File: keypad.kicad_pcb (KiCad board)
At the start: 2 copper layers, 76.3 x 115.3 mm, 104 parts, among them IC1 IS31FL3733-TQLS4, J1 Conn_01x04_Female, J3 B3FS-1002P, J4 USB_C_Receptacle_USB2.0, K1_1 KEYSW, K1_2 KEYSW, K1_3 KEYSW, K1_4 KEYSW, K2_1 KEYSW, K2_2 KEYSW, K2_3 KEYSW, K2_4 KEYSW, K3_1 KEYSW, K3_2 KEYSW, K3_3 KEYSW, K3_4 KEYSW, K4_1 KEYSW, K4_2 KEYSW, K4_3 KEYSW, K4_4 KEYSW, K5_1 KEYSW, K5_2 KEYSW, K5_3 KEYSW, U1 ATMEGA32U4, Y1 Crystal_GND24

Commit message: first manufactured version, testing needed
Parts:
- removed D12, D15, D17, D19, D20, D22: SK6805, LED_SMD:LED_SK6812MINI_PLCC4_3.5x3.5mm_P1.75mm
- added G***: LOGO, decals:science_badge, B.Cu at (173.5, 144.9)
- added G***: LOGO, decals:nostromo, B.Cu at (145.9, 99.8)
- J4: footprint Connector_USB:USB_C_Receptacle_Amphenol_12401548E4-2A_CircularHoles -> USB_C:Wuerth USB3.1 Type C Receptacle - Horizontal
- moved D16 14.5 mm to (111.7, 94.1)
- moved D13 14.3 mm to (179.5, 40.3)
- moved D14 13.6 mm to (114.6, 40.1)
- moved D23 12.6 mm to (181.2, 92.5)
- moved D18 11.5 mm to (111.5, 143.0)
- moved D21 9.45 mm to (179.6, 139.0)
- moved J4 5.07 mm to (142.7, 35.2)
- moved G*** 3.89 mm to (131.9, 55.8)
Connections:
- D13 pad 3: Net-(D12-Pad1) -> /led/UGLOW_LED
- D16 pad 3: Net-(D15-Pad1) -> Net-(D14-Pad1)
- D18 pad 3: Net-(D17-Pad1) -> Net-(D16-Pad1)
- D21 pad 3: Net-(D20-Pad1) -> Net-(D18-Pad1)
- D23 pad 3: Net-(D22-Pad1) -> Net-(D21-Pad1)
- J4 pad S1: GND -> (no net)
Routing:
- net Net-(D18-Pad1): track 30.5 -> 82.7 mm
- net Net-(D19-Pad1): track 34.5 -> 0.00 mm
- net Net-(D12-Pad1): track 30.1 -> 0.00 mm
- net Net-(D13-Pad1): track 35.2 -> 62.8 mm
- net +5V: track 477.7 -> 452.7 mm, vias 11 -> 10
- net Net-(D20-Pad1): track 24.1 -> 0.00 mm
- net Net-(D22-Pad1): track 24.0 -> 0.00 mm
- net GND: track 114.0 -> 90.3 mm, vias 44 -> 32
- net Net-(D21-Pad1): track 21.2 -> 44.5 mm
- net Net-(D14-Pad1): track 30.8 -> 52.9 mm
- net Net-(D15-Pad1): track 21.6 -> 0.00 mm
- net Net-(D17-Pad1): track 21.4 -> 0.00 mm
- net Net-(D16-Pad1): track 25.0 -> 46.2 mm
- net /led/UGLOW_LED: track 21.3 -> 7.16 mm
- net /CC1: track 13.8 -> 11.9 mm
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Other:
- board text added: "©FM 2019"

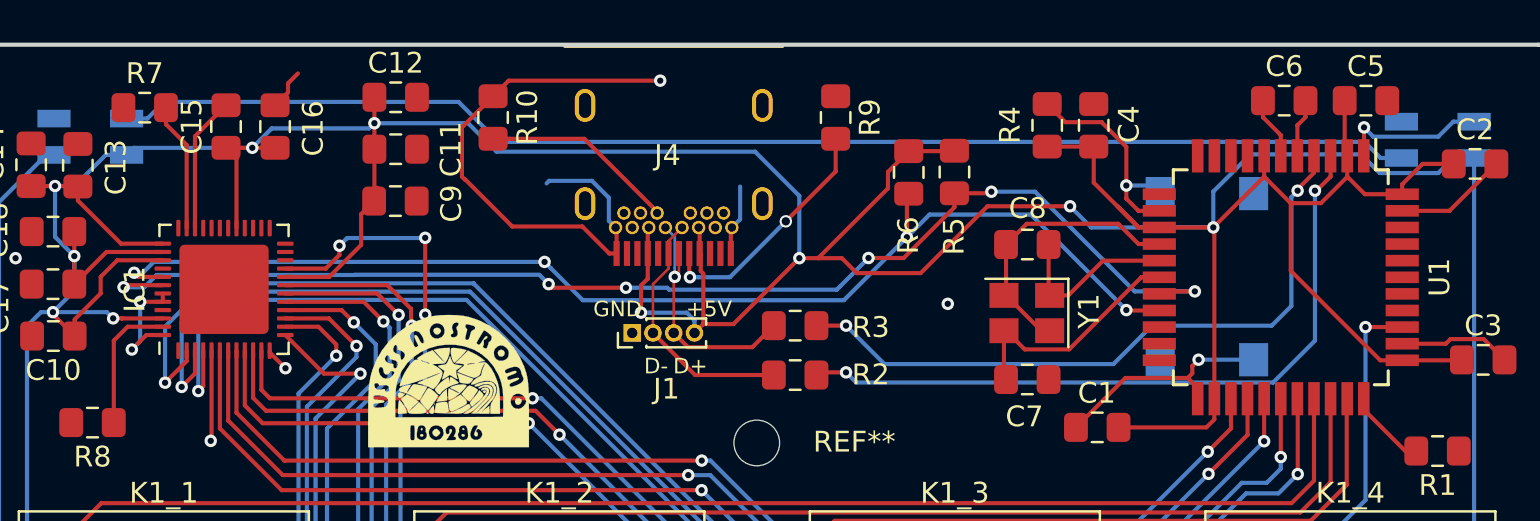
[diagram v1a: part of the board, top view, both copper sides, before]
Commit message: rerouted D+ and D- lines
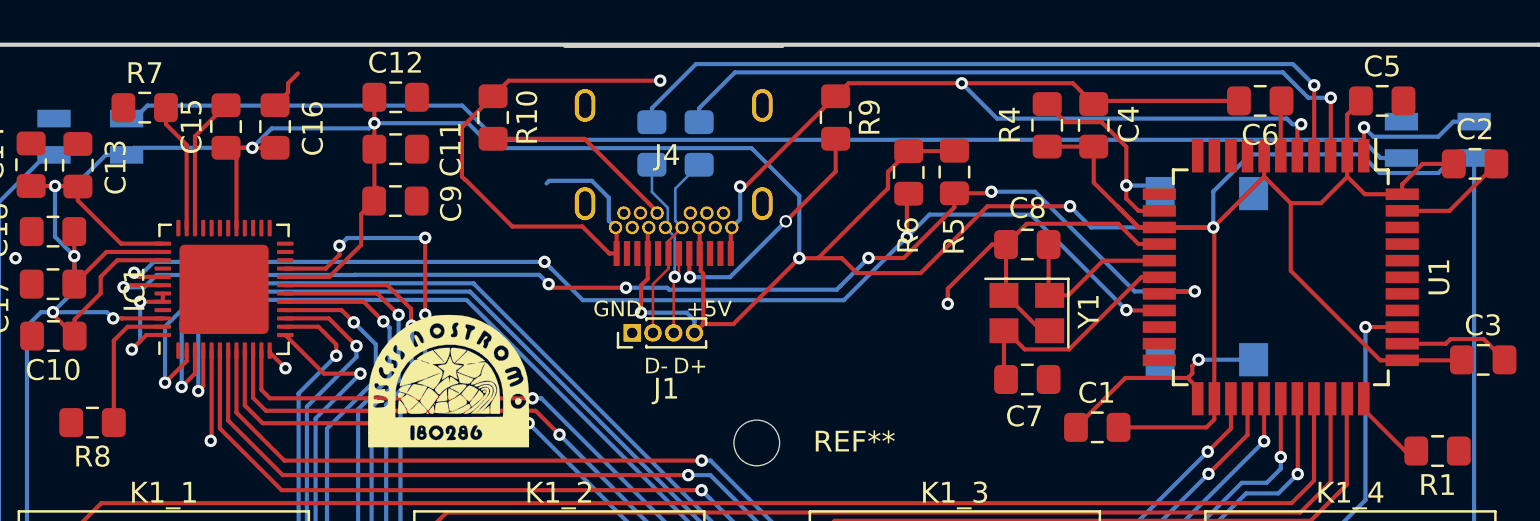
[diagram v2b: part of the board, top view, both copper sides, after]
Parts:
- R2, R3: moved to B.Cu
- moved R2 12.1 mm to (143.9, 40.5), turned to 270 degrees
- moved R3 11.2 mm to (141.7, 40.5), turned to 270 degrees
- moved C6 1.16 mm to (170.9, 38.4), turned to 180 degrees
- moved C5 0.78 mm to (176.8, 38.4)
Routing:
- net GND: track 90.3 -> 137.2 mm, vias 32 -> 35
- net Net-(R3-Pad1): track 32.5 -> 37.3 mm, vias 2 -> 1
- net /USB_D-: track 12.3 -> 9.29 mm
- net /USB_D+: track 12.0 -> 9.88 mm
- net Net-(R2-Pad1): track 34.4 -> 35.1 mm, vias 2 -> 1

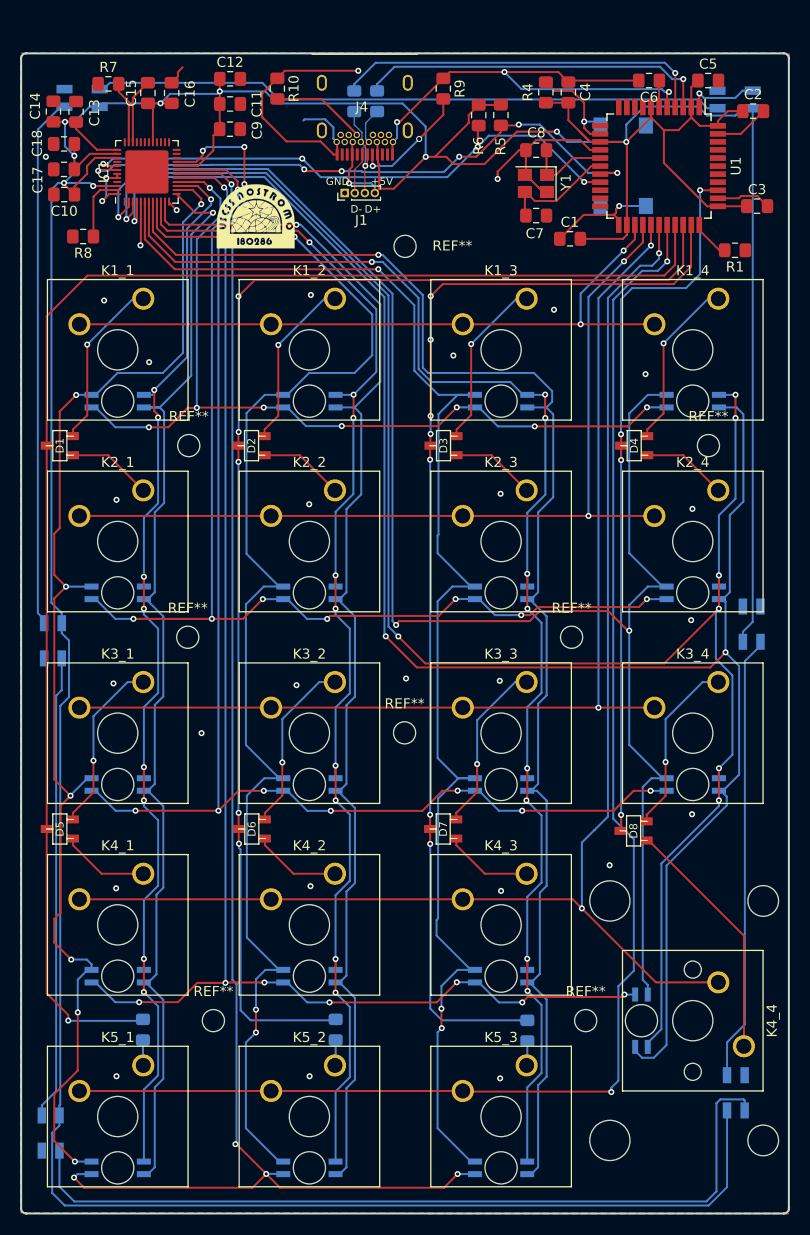
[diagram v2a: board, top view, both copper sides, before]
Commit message: Auf STM32F303 Controller umgestiegen. RGB per Switch rausgeflogen.
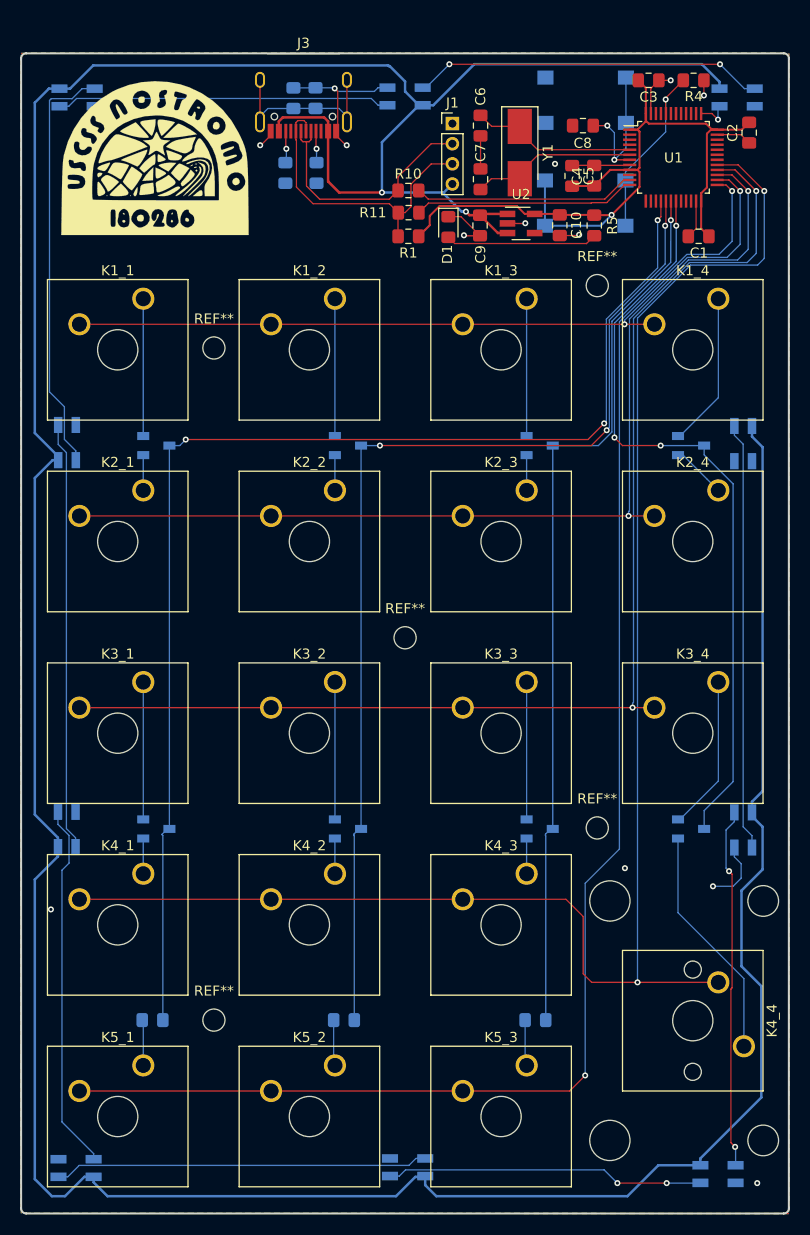
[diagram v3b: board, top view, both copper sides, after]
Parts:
- removed C12: 22uF, Capacitor_SMD:C_0805_2012Metric_Pad1.15x1.40mm_HandSolder
- removed C13, C15, C17: 0.1uF, Capacitor_SMD:C_0805_2012Metric_Pad1.15x1.40mm_HandSolder
- removed C14, C16, C18: 0.47uF, Capacitor_SMD:C_0805_2012Metric_Pad1.15x1.40mm_HandSolder
- removed D23: SK6805, LED_SMD:LED_SK6812MINI_PLCC4_3.5x3.5mm_P1.75mm
- removed D_LED_1, D_LED_10, D_LED_11, D_LED_12, D_LED_13, D_LED_14, D_LED_15, D_LED_16, D_LED_17, D_LED_18, D_LED_19, D_LED_2, D_LED_3, D_LED_4, D_LED_5, D_LED_6, D_LED_7, D_LED_8, D_LED_9: LED_RABG, reverse_RGB_LED:reverse_RGB_LED
- removed IC1: IS31FL3733-TQLS4, Package_DFN_QFN:QFN-48-1EP_6x6mm_P0.4mm_EP4.3x4.3mm
- removed J4: USB_C_Receptacle_USB2.0, USB_C:Wuerth USB3.1 Type C Receptacle - Horizontal
- removed R2, R3: 22, Resistor_SMD:R_0805_2012Metric_Pad1.15x1.40mm_HandSolder
- removed R9: 56k, Resistor_SMD:R_0805_2012Metric_Pad1.15x1.40mm_HandSolder
- removed the REF** at (146.7, 103.2)
- removed the REF** at (125.1, 93.8)
- removed the REF** at (163.2, 93.8)
- removed the REF** at (127.7, 131.8)
- removed the REF** at (164.7, 131.8)
- removed the REF** at (146.7, 54.9)
- removed the REF** at (125.2, 74.7)
- removed the REF** at (176.8, 74.7)
- added D12: D_x2_KCom_AAK, keyboard_parts:SOT23-3_HSOL, B.Cu at (175.1, 112.8)
- added D15: SK6805, LED_SMD:LED_SK6812MINI_PLCC4_3.5x3.5mm_P1.75mm, B.Cu at (114.1, 40.1)
- added D17: SK6805, LED_SMD:LED_SK6812MINI_PLCC4_3.5x3.5mm_P1.75mm, B.Cu at (113.1, 112.8)
- added D19: SK6805, LED_SMD:LED_SK6812MINI_PLCC4_3.5x3.5mm_P1.75mm, B.Cu at (146.9, 146.4)
- added D20: SK6805, LED_SMD:LED_SK6812MINI_PLCC4_3.5x3.5mm_P1.75mm, B.Cu at (177.8, 147.1)
- added D22: SK6805, LED_SMD:LED_SK6812MINI_PLCC4_3.5x3.5mm_P1.75mm, B.Cu at (180.3, 74.5)
- added R11: 22, Resistor_SMD:R_0805_2012Metric_Pad1.15x1.40mm_HandSolder, F.Cu at (147.1, 51.5)
- added REF**: MountingHole_2.2mm_M2_DIN965, MountingHole:MountingHole_2.2mm_M2_DIN965, F.Cu at (127.7, 65.0)
- added REF**: MountingHole_2.2mm_M2_DIN965, MountingHole:MountingHole_2.2mm_M2_DIN965, F.Cu at (165.8, 58.8)
- added REF**: MountingHole_2.2mm_M2_DIN965, MountingHole:MountingHole_2.2mm_M2_DIN965, F.Cu at (127.7, 131.8)
- added REF**: MountingHole_2.2mm_M2_DIN965, MountingHole:MountingHole_2.2mm_M2_DIN965, F.Cu at (165.8, 112.7)
- added REF**: MountingHole_2.2mm_M2_DIN965, MountingHole:MountingHole_2.2mm_M2_DIN965, F.Cu at (146.7, 93.8)
- added SW1: SW_Push_Dual, SMD_Switch:B3FS-1002P, B.Cu at (164.6, 50.6)
- added SW2: SW_Push_Dual, SMD_Switch:B3FS-1002P, B.Cu at (164.7, 40.4)
- added U2: MCP1804x-3302xOT, Package_TO_SOT_SMD:SOT-23-5_HandSoldering, F.Cu at (158.2, 52.6)
- C10: value 0.47u -> 10u
- C11: value 0.47uF -> 4.7n; moved to B.Cu
- C6: value 1u -> 18p
- C7: value 22p -> 18p
- C8: value 22p -> 0.1u
- C9: value 0.1uF -> 10u
- D1: value D_x2_KCom_AAK -> POWER_LED; footprint keyboard_parts:SOT23-3_HSOL -> LED_SMD:LED_0805_2012Metric_Pad1.15x1.40mm_HandSolder
- D11, D9: value D -> D_x2_KCom_AAK; footprint Diode_SMD:D_0805_2012Metric_Pad1.15x1.40mm_HandSolder -> keyboard_parts:SOT23-3_HSOL
- D2, D3, D5, D6, D8: moved to B.Cu
- D4, D7: value D_x2_KCom_AAK -> D; footprint keyboard_parts:SOT23-3_HSOL -> Diode_SMD:D_0805_2012Metric_Pad1.15x1.40mm_HandSolder; moved to B.Cu
- J1: footprint Connector_PinHeader_1.00mm:PinHeader_1x04_P1.00mm_Vertical -> Connector_PinHeader_2.00mm:PinHeader_1x04_P2.00mm_Vertical
- J3: value B3FS-1002P -> USB_C_Receptacle_USB2.0; footprint SMD_Switch:B3FS-1002P -> USB_C:USB C HRQ low cost; moved to F.Cu
- R1: value 10k -> 1.5k
- R10: value 56k -> 22
- R5: value 1k -> 330
- R6: value 1k -> 1M; moved to B.Cu
- R7: value 20k -> 5.1k; moved to B.Cu
- R8: value 100k -> 5.1k; moved to B.Cu
- U1: value ATMEGA32U4 -> STM32F303C6Tx; footprint Package_QFP:LQFP-44_10x10mm_P0.8mm -> Package_QFP:LQFP-48_7x7mm_P0.5mm
- Y1: value Crystal_GND24 -> A7 8MHz; footprint Crystal:Crystal_SMD_Abracon_ABM8G-4Pin_3.2x2.5mm -> Crystal:Crystal_SMD_5032-2Pin_5.0x3.2mm_HandSoldering
- moved D4 74.5 mm to (121.6, 131.8), turned to 180 degrees
- moved D11 60.4 mm to (175.1, 74.7), turned to 90 degrees
- moved C10 49.3 mm to (162.1, 52.8), turned to 270 degrees
- moved D5 47.7 mm to (141.0, 74.7)
- moved D3 47.6 mm to (122.0, 112.8)
- moved G*** 47.5 mm to (126.3, 139.9)
- moved D1 44.3 mm to (151.0, 53.0), turned to 270 degrees
- moved D9 44.2 mm to (160.1, 112.8), turned to 90 degrees
- moved D8 39.4 mm to (160.1, 74.7)
- moved J3 32.9 mm to (136.6, 38.4), turned to 180 degrees
- moved R1 32.5 mm to (147.0, 53.9)
- moved D14 32.1 mm to (146.7, 40.0)
- moved C9 26.6 mm to (154.2, 52.8), turned to 270 degrees
- moved D21 26.1 mm to (180.3, 112.9), turned to 90 degrees
- moved R7 22.5 mm to (137.9, 47.6), turned to 270 degrees
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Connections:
- C1 pad 1: +5V -> GND
- C1 pad 2: GND -> +3V3
- C10 pad 1: +5V -> +3V3
- C11 pad 1: +5V -> Net-(C11-Pad1)
- C2 pad 1: +5V -> GND
- C2 pad 2: GND -> +3V3
- C3 pad 1: +5V -> GND
- C3 pad 2: GND -> +3V3
- C4 pad 1: +5V -> GND
- C4 pad 2: GND -> +3V3
- C5 pad 1: +5V -> GND
- C5 pad 2: GND -> +3V3
- C6 pad 1: Net-(C6-Pad1) -> GND
- C6 pad 2: GND -> OSC_IN
- C7 pad 1: Net-(C7-Pad1) -> GND
- C7 pad 2: GND -> OSC_OUT
- C8 pad 1: Net-(C8-Pad1) -> GND
- C8 pad 2: GND -> NRST
- C9 pad 1: +5V -> VBUS
- D1 pad 1: Net-(D1-Pad1) -> GND
- D10 pad 1: Col2 -> Col3
- D11 pad 1: Col3 -> Net-(D11-Pad1)
- D13 pad 4: +5V -> VBUS
- D14 pad 4: +5V -> VBUS
- D16 pad 3: Net-(D14-Pad1) -> Net-(D15-Pad1)
- D16 pad 4: +5V -> VBUS
- D18 pad 3: Net-(D16-Pad1) -> Net-(D17-Pad1)
- D18 pad 4: +5V -> VBUS
- D2 pad 3: Col2 -> Col1
- D21 pad 3: Net-(D18-Pad1) -> Net-(D20-Pad1)
- D21 pad 4: +5V -> VBUS
- D3 pad 3: Col3 -> Col1
- D4 pad 1: Net-(D4-Pad1) -> Col1
- D5 pad 3: Col1 -> Col2
- D7 pad 1: Net-(D7-Pad1) -> Col2
- D8 pad 3: Col4 -> Col3
- D9 pad 1: Col1 -> Net-(D9-Pad1)
- J1 pad 2: /USB_D- -> USB_N
- J1 pad 3: /USB_D+ -> USB_P
- J1 pad 4: +5V -> VBUS
- K1_1 pad 1: Net-(D1-Pad2) -> Net-(D2-Pad2)
- K1_2 pad 1: Net-(D2-Pad2) -> Net-(D5-Pad2)
- K1_3 pad 1: Net-(D3-Pad2) -> Net-(D8-Pad2)
- K1_4 pad 1: Net-(D4-Pad2) -> Net-(D11-Pad2)
- K2_1 pad 1: Net-(D1-Pad1) -> Net-(D2-Pad1)
- K2_2 pad 1: Net-(D2-Pad1) -> Net-(D5-Pad1)
- K2_3 pad 1: Net-(D3-Pad1) -> Net-(D8-Pad1)
- K2_4 pad 1: Net-(D4-Pad1) -> Net-(D11-Pad1)
- K3_1 pad 1: Net-(D5-Pad2) -> Net-(D3-Pad2)
- K3_3 pad 1: Net-(D7-Pad2) -> Net-(D9-Pad2)
- K3_4 pad 1: Net-(D8-Pad2) -> Net-(D12-Pad2)
- K4_1 pad 1: Net-(D5-Pad1) -> Net-(D3-Pad1)
- K4_3 pad 1: Net-(D7-Pad1) -> Net-(D9-Pad1)
- K4_4 pad 1: Net-(D8-Pad1) -> Net-(D12-Pad1)
- K5_1 pad 1: Net-(D9-Pad2) -> Net-(D4-Pad2)
- K5_2 pad 1: Net-(D10-Pad2) -> Net-(D7-Pad2)
- K5_3 pad 1: Net-(D11-Pad2) -> Net-(D10-Pad2)
- R1 pad 1: GND -> +3V3
- R1 pad 2: Net-(R1-Pad2) -> USB_P
- R10 pad 1: GND -> Net-(R10-Pad1)
- R10 pad 2: /CC2 -> USB_N
- R4 pad 1: Net-(J3-Pad1) -> GND
- R4 pad 2: +5V -> BOOT
- R5 pad 1: +5V -> Net-(D1-Pad2)
- R5 pad 2: /led/led_scl -> +3V3
- R6 pad 1: +5V -> GND
- R6 pad 2: /led/led_sda -> Net-(C11-Pad1)
- R7 pad 1: GND -> Net-(J3-PadA5)
- R7 pad 2: Net-(IC1-Pad35) -> GND
- R8 pad 1: Net-(IC1-Pad47) -> Net-(J3-PadB5)
- U1 pad 1: /led/UGLOW_LED -> +3V3
- U1 pad 11: (no net) -> Net-(R10-Pad1)
- U1 pad 12: (no net) -> Net-(R11-Pad1)
- U1 pad 13: Net-(J3-Pad1) -> (no net)
- U1 pad 14: +5V -> (no net)
- U1 pad 15: GND -> (no net)
- U1 pad 16: Net-(C8-Pad1) -> Col1
- U1 pad 17: Net-(C7-Pad1) -> Col2
- U1 pad 18: /led/led_scl -> Col3
- U1 pad 19: /led/led_sda -> Col4
- U1 pad 2: +5V -> (no net)
- U1 pad 24: +5V -> +3V3
- U1 pad 25: Row1 -> Row5
- U1 pad 26: Row2 -> Row1
- U1 pad 27: Row3 -> Row2
- U1 pad 28: Row4 -> Row3
- U1 pad 29: Row5 -> Row4
- U1 pad 3: Net-(R2-Pad1) -> (no net)
- U1 pad 30: Col1 -> (no net)
- U1 pad 31: Col2 -> (no net)
- U1 pad 32: Col3 -> (no net)
- U1 pad 33: Net-(R1-Pad2) -> (no net)
- U1 pad 34: +5V -> (no net)
- U1 pad 36: Col4 -> +3V3
- U1 pad 37: (no net) -> /led/UGLOW_LED
- U1 pad 4: Net-(R3-Pad1) -> (no net)
- U1 pad 43: GND -> (no net)
- U1 pad 44: +5V -> BOOT
- U1 pad 5: GND -> OSC_IN
- U1 pad 6: Net-(C6-Pad1) -> OSC_OUT
- U1 pad 7: +5V -> NRST
- U1 pad 8: (no net) -> GND
- U1 pad 9: (no net) -> +3V3
- Y1 pad 1: Net-(C8-Pad1) -> OSC_IN
- Y1 pad 2: GND -> OSC_OUT
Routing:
- net +5V: track 453.1 -> 0.00 mm, vias 10 -> 0
- net VBUS: track 0.00 -> 383.5 mm, vias 0 -> 2
- net /led/SW3: track 180.8 -> 0.00 mm, vias 3 -> 0
- net /led/SW2: track 179.9 -> 0.00 mm, vias 8 -> 0
- net /led/SW1: track 166.0 -> 0.00 mm, vias 3 -> 0
- net /led/CS5: track 157.3 -> 0.00 mm, vias 7 -> 0
- net /led/CS4: track 145.2 -> 0.00 mm, vias 8 -> 0
- net /led/SW4: track 141.4 -> 0.00 mm, vias 3 -> 0
- net /led/SW6: track 141.3 -> 0.00 mm, vias 1 -> 0
- net /led/SW5: track 137.4 -> 0.00 mm, vias 9 -> 0
- net /led/SW7: track 135.8 -> 0.00 mm, vias 3 -> 0
- net /led/CS3: track 130.8 -> 0.00 mm, vias 8 -> 0
- net /led/SW9: track 123.3 -> 0.00 mm, vias 1 -> 0
- net /led/SW10: track 122.8 -> 0.00 mm, vias 7 -> 0
- net /led/SW8: track 122.3 -> 0.00 mm, vias 9 -> 0
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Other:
- net class Default: clearance 0.2 -> 0.127; trace_width 0.2 -> 0.127
- net class VCC GND: clearance 0.508 -> 0.27; trace_width 0.254 -> 0.25
- rule trace_clearance: 0.2 -> 0.127
- board text added: "USCSS NOSTROMO 180286 V 1.1"
- board text removed: "+5V"
- board text removed: "D+"
- board text removed: "D-"
- board text removed: "GND"
- board text removed: "USCSS NOSTROMO 180286 V 1.0"

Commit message: USB war an falschem Pin. Fixed! Boot und Reset geaendert. Anderer Resetbutton
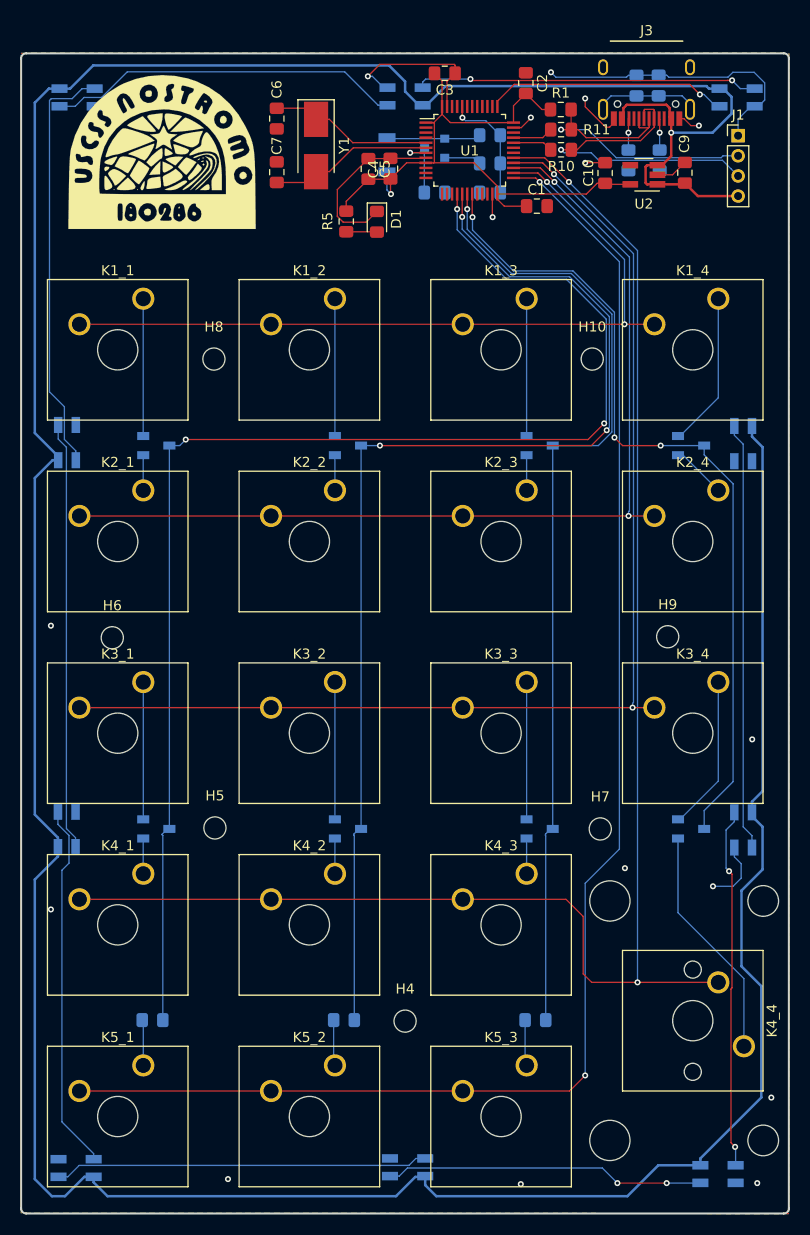
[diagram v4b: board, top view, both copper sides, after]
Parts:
- removed G***: LOGO, decals:nostromo_batch
- removed G***: LOGO, decals:nostromo
- removed G***: LOGO, decals:science_badge
- removed R4: 10k, Resistor_SMD:R_0805_2012Metric_Pad1.15x1.40mm_HandSolder
- removed REF** (x5): MountingHole_2.2mm_M2_DIN965, MountingHole:MountingHole_2.2mm_M2_DIN965
- removed SW2: SW_Push_Dual, SMD_Switch:B3FS-1002P
- added C12: 4.7u, Capacitor_SMD:C_0805_2012Metric_Pad1.15x1.40mm_HandSolder, B.Cu at (155.1, 49.6)
- added D23: 1N4148, Diode_SMD:D_0805_2012Metric_Pad1.15x1.40mm_HandSolder, B.Cu at (155.1, 43.9)
- added H1: Batch, decals:nostromo_batch, F.Cu at (122.6, 54.9)
- added H10: MountingHole, MountingHole:MountingHole_2.2mm_M2, F.Cu at (165.3, 66.1)
- added H2: Nostromo, decals:nostromo, B.Cu at (145.7, 97.0)
- added H3: Science, decals:science_badge, B.Cu at (131.0, 145.8)
- added H4: MountingHole, MountingHole:MountingHole_2.2mm_M2, F.Cu at (146.7, 131.9)
- added H5: MountingHole, MountingHole:MountingHole_2.2mm_M2, F.Cu at (127.8, 112.7)
- added H6: MountingHole, MountingHole:MountingHole_2.2mm_M2, F.Cu at (117.6, 93.8)
- added H7: MountingHole, MountingHole:MountingHole_2.2mm_M2, F.Cu at (166.1, 112.8)
- added H8: MountingHole, MountingHole:MountingHole_2.2mm_M2, F.Cu at (127.7, 66.1)
- added H9: MountingHole, MountingHole:MountingHole_2.2mm_M2, F.Cu at (172.8, 93.7)
- added Q1: BC847, Package_TO_SOT_SMD:SOT-23, B.Cu at (149.6, 45.1)
- added R2: 100k, Resistor_SMD:R_0805_2012Metric_Pad1.15x1.40mm_HandSolder, B.Cu at (155.1, 46.7)
- C8: value 0.1u -> 4.7u; moved to B.Cu
- SW1: value SW_Push_Dual -> SW_Push; footprint SMD_Switch:B3FS-1002P -> Button_Switch_SMD:SW_SPST_B3U-1000P
- moved C11 34.1 mm to (171.9, 38.9)
- moved J3 34.1 mm to (170.7, 37.1)
- moved R6 34.1 mm to (169.7, 38.9)
- moved R7 34.1 mm to (172.0, 46.4)
- moved R8 34.1 mm to (168.9, 46.4)
- moved J1 28.4 mm to (179.8, 43.9)
- moved R5 24.7 mm to (140.9, 52.4)
- moved C2 22.7 mm to (158.7, 38.7), turned to 270 degrees
- moved C9 21.0 mm to (174.5, 47.6), turned to 90 degrees
- moved SW1 20.3 mm to (144.9, 45.8), turned to 90 degrees
- moved C3 20.3 mm to (150.7, 37.7)
- moved C4 20.3 mm to (145.2, 47.2)
- moved C5 20.3 mm to (143.1, 47.2)
- moved C6 20.3 mm to (133.9, 42.2)
- moved C7 20.3 mm to (133.9, 47.5)
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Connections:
- J1 pad 2: USB_N -> USB_P
- J1 pad 3: USB_P -> USB_N
- SW1 pad 2: BOOT -> Net-(D23-Pad2)
- U1 pad 11: Net-(R10-Pad1) -> (no net)
- U1 pad 12: Net-(R11-Pad1) -> (no net)
- U1 pad 32: (no net) -> Net-(R10-Pad1)
- U1 pad 33: (no net) -> Net-(R11-Pad1)
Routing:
- net GND: track 56.3 -> 89.7 mm, vias 13 -> 16
- net /led/UGLOW_LED: track 3.31 -> 24.2 mm
- net Net-(R10-Pad1): track 22.1 -> 3.99 mm
- net Net-(R11-Pad1): track 22.1 -> 4.03 mm
- net +3V3: track 79.2 -> 64.9 mm
- net VBUS: track 383.5 -> 370.1 mm, vias 2 -> 1
- net Net-(D1-Pad2): track 15.1 -> 3.06 mm
- net Net-(D23-Pad2): track 0.00 -> 9.41 mm
- net Net-(C11-Pad1): track 19.1 -> 10.4 mm
- net Col1: track 126.1 -> 134.2 mm
- net Col2: track 107.8 -> 115.7 mm
- net Col3: track 89.4 -> 97.1 mm
- net NRST: track 15.3 -> 7.63 mm, vias 2 -> 1
- net Col4: track 75.8 -> 83.3 mm
- net USB_N: track 25.4 -> 32.5 mm, vias 0 -> 1
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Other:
- board text added: "USCSS NOSTROMO 180286 V 1.2"
- board text removed: "USCSS NOSTROMO 180286 V 1.1"
